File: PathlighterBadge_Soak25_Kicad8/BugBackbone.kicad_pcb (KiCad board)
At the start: 2 copper layers, 21.7 x 75.4 mm, 4 parts

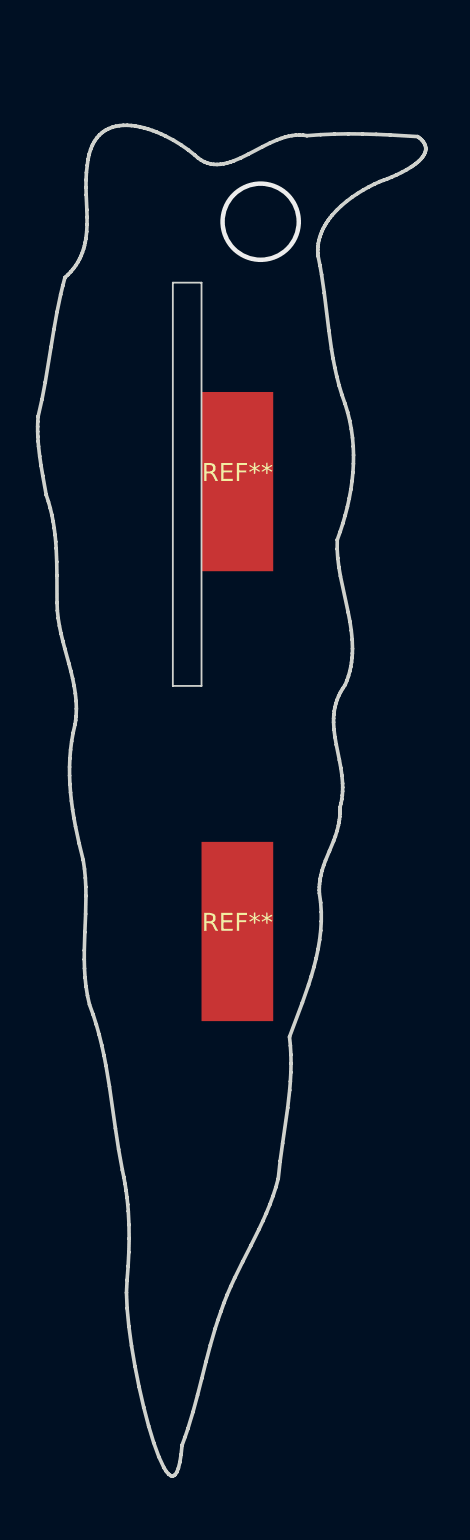
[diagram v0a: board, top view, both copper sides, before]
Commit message: Flip slots again, move logos
Slot's gotta be this way so there's room for the LED
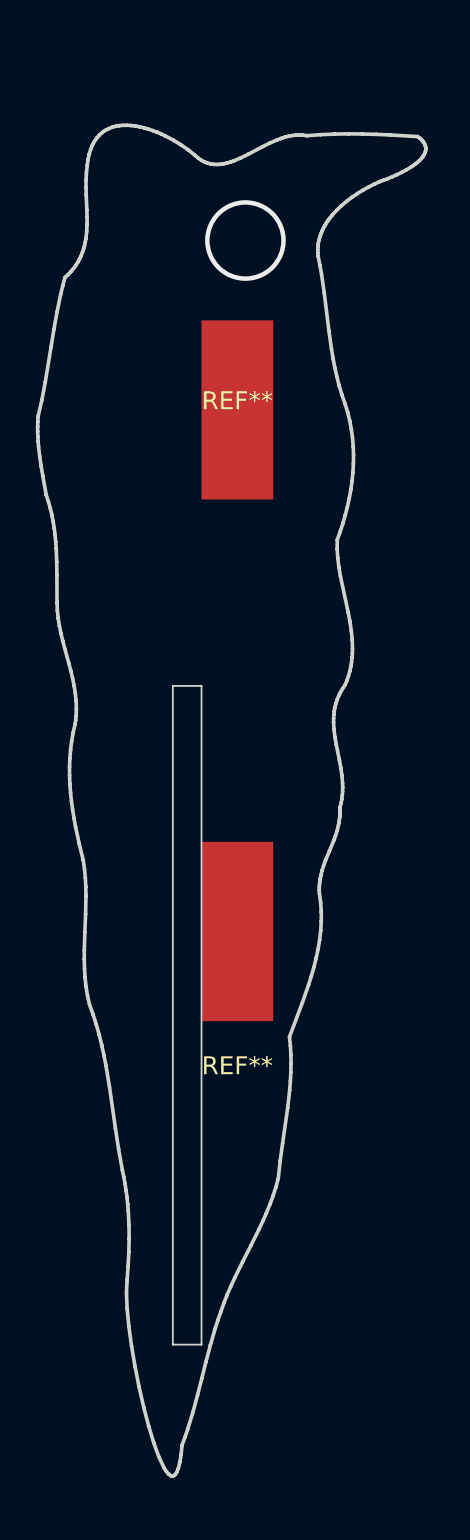
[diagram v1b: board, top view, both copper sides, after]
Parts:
- removed the ? at (108.2, 54.9)
- moved ? 67.2 mm to (105.2, 128.0)
- moved REF** 8.00 mm to (108.0, 109.0)
- moved REF** 4.00 mm to (108.0, 72.0)
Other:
- outline, holes or cut-outs redrawn
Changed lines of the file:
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@@
 (kicad_pcb
-	(version 20240108)
+	(version 20241229)
 	(generator "pcbnew")
-	(generator_version "8.0")
+	(generator_version "9.0")
 	(general
 		(thickness 1.6)
@@
 	(layers
 		(0 "F.Cu" signal)
-		(31 "B.Cu" signal)
-		(32 "B.Adhes" user "B.Adhesive")
-		(33 "F.Adhes" user "F.Adhesive")
-		(34 "B.Paste" user)
-		(35 "F.Paste" user)
-		(36 "B.SilkS" user "B.Silkscreen")
-		(37 "F.SilkS" user "F.Silkscreen")
-		(38 "B.Mask" user)
-		(39 "F.Mask" user)
-		(40 "Dwgs.User" user "User.Drawings")
-		(41 "Cmts.User" user "User.Comments")
-		(42 "Eco1.User" user "User.Eco1")
-		(43 "Eco2.User" user "User.Eco2")
-		(44 "Edge.Cuts" user)
-		(45 "Margin" user)
-		(46 "B.CrtYd" user "B.Courtyard")
-		(47 "F.CrtYd" user "F.Courtyard")
-		(48 "B.Fab" user)
-		(49 "F.Fab" user)
-		(50 "User.1" user)
-		(51 "User.2" user)
-		(52 "User.3" user)
-		(53 "User.4" user)
-		(54 "User.5" user)
-		(55 "User.6" user)
-		(56 "User.7" user)
-		(57 "User.8" user)
-		(58 "User.9" user)
+		(2 "B.Cu" signal)
+		(9 "F.Adhes" user "F.Adhesive")
+		(11 "B.Adhes" user "B.Adhesive")
+		(13 "F.Paste" user)
+		(15 "B.Paste" user)
+		(5 "F.SilkS" user "F.Silkscreen")
+		(7 "B.SilkS" user "B.Silkscreen")
+		(1 "F.Mask" user)
+		(3 "B.Mask" user)
+		(17 "Dwgs.User" user "User.Drawings")
+		(19 "Cmts.User" user "User.Comments")
+		(21 "Eco1.User" user "User.Eco1")
+		(23 "Eco2.User" user "User.Eco2")
+		(25 "Edge.Cuts" user)
+		(27 "Margin" user)
+		(31 "F.CrtYd" user "F.Courtyard")
+		(29 "B.CrtYd" user "B.Courtyard")
+		(35 "F.Fab" user)
+		(33 "B.Fab" user)
+		(39 "User.1" user)
+		(41 "User.2" user)
+		(43 "User.3" user)
+		(45 "User.4" user)
+		(47 "User.5" user)
+		(49 "User.6" user)
+		(51 "User.7" user)
+		(53 "User.8" user)
+		(55 "User.9" user)
 	)
 	(setup
 		(pad_to_mask_clearance 0)
 		(allow_soldermask_bridges_in_footprints no)
+		(tenting front back)
 		(grid_origin 105.25 85.75)
 		(pcbplotparams
-			(layerselection 0x00010fc_ffffffff)
-			(plot_on_all_layers_selection 0x0000000_00000000)
+			(layerselection 0x00000000_00000000_55555555_5755f5ff)
+			(plot_on_all_layers_selection 0x00000000_00000000_00000000_00000000)
 			(disableapertmacros no)
 			(usegerberextensions no)
@@
 			(svgprecision 4)
 			(plotframeref no)
-			(viasonmask no)
 			(mode 1)
 			(useauxorigin no)
@@
 			(pdf_front_fp_property_popups yes)
 			(pdf_back_fp_property_popups yes)
+			(pdf_metadata yes)
+			(pdf_single_document no)
 			(dxfpolygonmode yes)
 			(dxfimperialunits yes)
@@
 			(psnegative no)
 			(psa4output no)
-			(plotreference yes)
-			(plotvalue yes)
-			(plotfptext yes)
+			(plot_black_and_white yes)
 			(plotinvisibletext no)
 			(sketchpadsonfab no)
+			(plotpadnumbers no)
+			(hidednponfab no)
+			(sketchdnponfab yes)
+			(crossoutdnponfab yes)
 			(subtractmaskfromsilk no)
 			(outputformat 1)
@@
 	(footprint "adhoc:MechanicalJoint"
 		(layer "F.Cu")
-		(at 108.05 101.05)
+		(at 108.05 109.05)
 		(property "Reference" "REF**"
 			(at 0 -0.5 0)
@@
 			(unlocked yes)
 			(layer "F.Fab")
-			(effects
-				(font
-					(size 1 1)
-					(thickness 0.15)
-				)
-			)
-		)
-		(property "Footprint" "adhoc:MechanicalJoint"
-			(at 0 0 0)
-			(unlocked yes)
-			(layer "F.Fab")
-			(hide yes)
 			(effects
 				(font
@@
 		)
 		(pad "" smd rect
-			(at 0 0)
+			(at 0 -8)
 			(size 4 10)
-			(layers "F.Cu" "F.Paste" "F.Mask")
-		)
+			(layers "F.Cu" "F.Mask" "F.Paste")
+		)
+		(embedded_fonts no)
 	)
 	(footprint "adhoc:Slot_1.6mm"
 		(layer "F.Cu")
-		(at 108.25 54.85 135)
+		(at 105.25 128)
 		(property "Reference" ""
-			(at 0 0 135)
+			(at 0 0 0)
 			(layer "F.SilkS")
 			(effects
@@
 		)
 		(property "Value" ""
-			(at 0 0 135)
-			(layer "F.Fab")
-			(effects
-				(font
-					(size 1.27 1.27)
-					(thickness 0.15)
-				)
-			)
-		)
-		(property "Footprint" "adhoc:Slot_1.6mm"
-			(at 0 0 135)
-			(layer "F.Fab")
-			(hide yes)
-			(effects
-				(font
-					(size 1.27 1.27)
-					(thickness 0.15)
-				)
-			)
-		)
-		(property "Datasheet" ""
-			(at 0 0 135)
-			(layer "F.Fab")
-			(hide yes)
-			(effects
-				(font
-					(size 1.27 1.27)
-					(thickness 0.15)
-				)
-			)
-		)
-		(property "Description" ""
-			(at 0 0 135)
-			(layer "F.Fab")
-			(hide yes)
-			(effects
-				(font
-					(size 1.27 1.27)
-					(thickness 0.15)
-				)
-			)
-		)
-		(pad "" np_thru_hole circle
-			(at 0 0 135)
-			(size 1.6 1.6)
-			(drill oval 1.6 10)
-			(layers "*.Cu" "*.Mask" "In1.Cu" "In2.Cu" "In3.Cu" "In4.Cu" "In5.Cu" "In6.Cu"
-				"In7.Cu" "In8.Cu" "In9.Cu" "In10.Cu" "In11.Cu" "In12.Cu" "In13.Cu" "In14.Cu"
-				"In15.Cu" "In16.Cu" "In17.Cu" "In18.Cu" "In19.Cu" "In20.Cu" "In21.Cu"
-				"In22.Cu" "In23.Cu" "In24.Cu" "In25.Cu" "In26.Cu" "In27.Cu" "In28.Cu"
-				"In29.Cu" "In30.Cu"
-			)
-		)
-	)
-	(footprint "adhoc:Slot_1.6mm"
-		(layer "F.Cu")
-		(at 105.25 60.75)
-		(property "Reference" ""
-			(at 0 0 0)
-			(layer "F.SilkS")
-			(effects
-				(font
-					(size 1.27 1.27)
-					(thickness 0.15)
-				)
-			)
-		)
-		(property "Value" ""
-			(at 0 0 0)
-			(layer "F.Fab")
-			(effects
-				(font
-					(size 1.27 1.27)
-					(thickness 0.15)
-				)
-			)
-		)
-		(property "Footprint" "adhoc:Slot_1.6mm"
-			(at 0 0 0)
-			(layer "F.Fab")
-			(hide yes)
+			(at 0 0 0)
+			(layer "F.Fab")
 			(effects
 				(font
@@
 			(size 1.6 1.6)
 			(drill oval 1.6 10)
-			(layers "*.Cu" "*.Mask" "In1.Cu" "In2.Cu" "In3.Cu" "In4.Cu" "In5.Cu" "In6.Cu"
-				"In7.Cu" "In8.Cu" "In9.Cu" "In10.Cu" "In11.Cu" "In12.Cu" "In13.Cu" "In14.Cu"
-				"In15.Cu" "In16.Cu" "In17.Cu" "In18.Cu" "In19.Cu" "In20.Cu" "In21.Cu"
-				"In22.Cu" "In23.Cu" "In24.Cu" "In25.Cu" "In26.Cu" "In27.Cu" "In28.Cu"
-				"In29.Cu" "In30.Cu"
-			)
-		)
+			(layers "*.Cu" "*.Mask")
+		)
+		(embedded_fonts no)
 	)
 	(footprint "adhoc:MechanicalJoint"
 		(layer "F.Cu")
-		(at 108.05 75.95)
+		(at 108.05 71.95)
 		(property "Reference" "REF**"
 			(at 0 -0.5 0)
@@
 			(unlocked yes)
 			(layer "F.Fab")
-			(effects
-				(font
-					(size 1 1)
-					(thickness 0.15)
-				)
-			)
-		)
-		(property "Footprint" "adhoc:MechanicalJoint"
-			(at 0 0 0)
-			(unlocked yes)
-			(layer "F.Fab")
-			(hide yes)
 			(effects
 				(font
@@
 			(at 0 0)
 			(size 4 10)
-			(layers "F.Cu" "F.Paste" "F.Mask")
-		)
+			(layers "F.Cu" "F.Mask" "F.Paste")
+		)
+		(embedded_fonts no)
 	)
 	(gr_poly
@@
 			(type solid)
 		)
-		(fill none)
+		(fill no)
 		(layer "Edge.Cuts")
 	)
 	(gr_rect
-		(start 104.45 64.85)
-		(end 106.05 87.35)
+		(start 104.45 87.35)
+		(end 106.05 124.1)
 		(stroke
 			(width 0.1)
 			(type default)
 		)
-		(fill none)
+		(fill no)
 		(layer "Edge.Cuts")
 	)
 	(via
-		(at 109.35 61.45)
+		(at 108.5 62.5)
 		(size 4.5)
 		(drill 4)
@@
 		(net 0)
 	)
+	(embedded_fonts no)
 )

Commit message: Rework backbone
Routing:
- added copper zone on F.Cu, net (none)
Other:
- board size 21.7 x 75.4 mm -> 22 x 75.3 mm

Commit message: Tweaks from feedback
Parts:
- removed the REF** at (108.0, 109.0)
- added REF**: MechanicalJoint, footprints:MechanicalJoint, B.Cu at (108.0, 97.5)
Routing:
- removed copper zone on F.Cu, net (none)
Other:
- board size 22 x 75.3 mm -> 22 x 71.3 mm

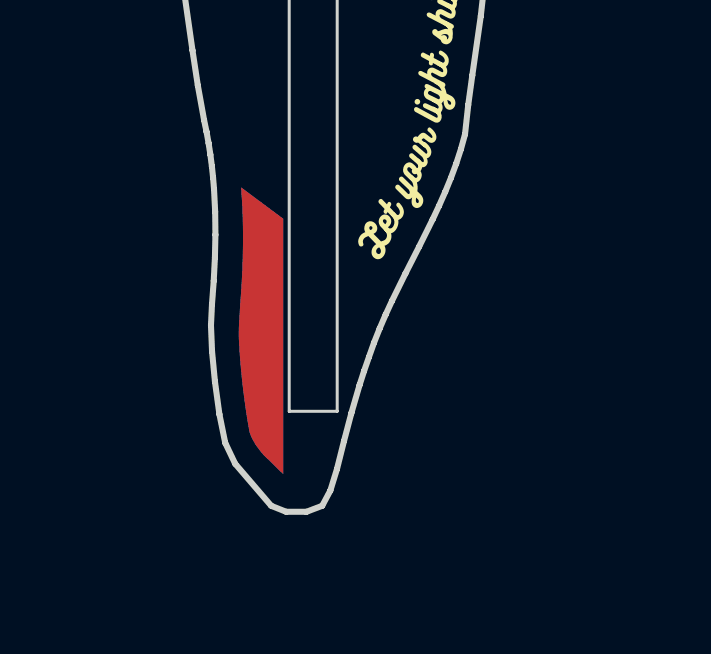
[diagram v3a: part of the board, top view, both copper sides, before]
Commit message: Fix overlap on G/C, adjust backbone bands
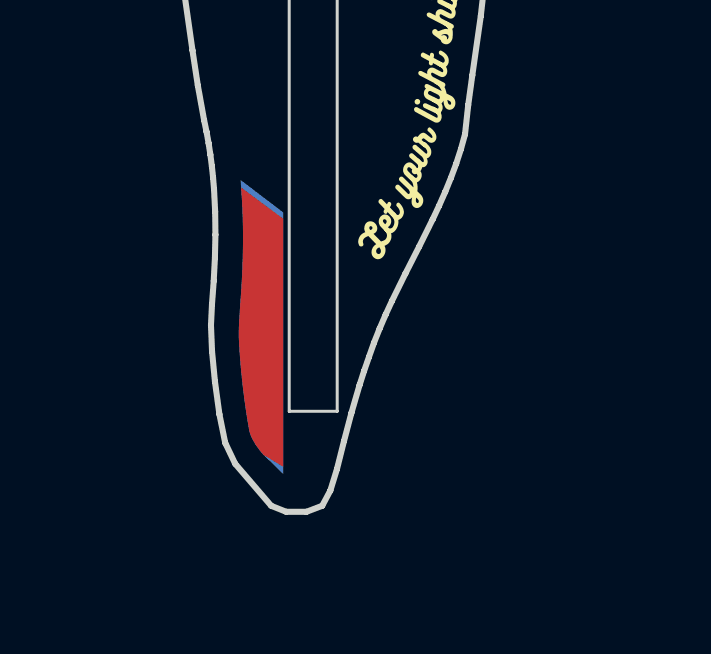
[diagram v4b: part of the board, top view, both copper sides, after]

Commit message: Final tweaks, hopefully!
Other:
- board size 22 x 71.3 mm -> 18.6 x 70.3 mm

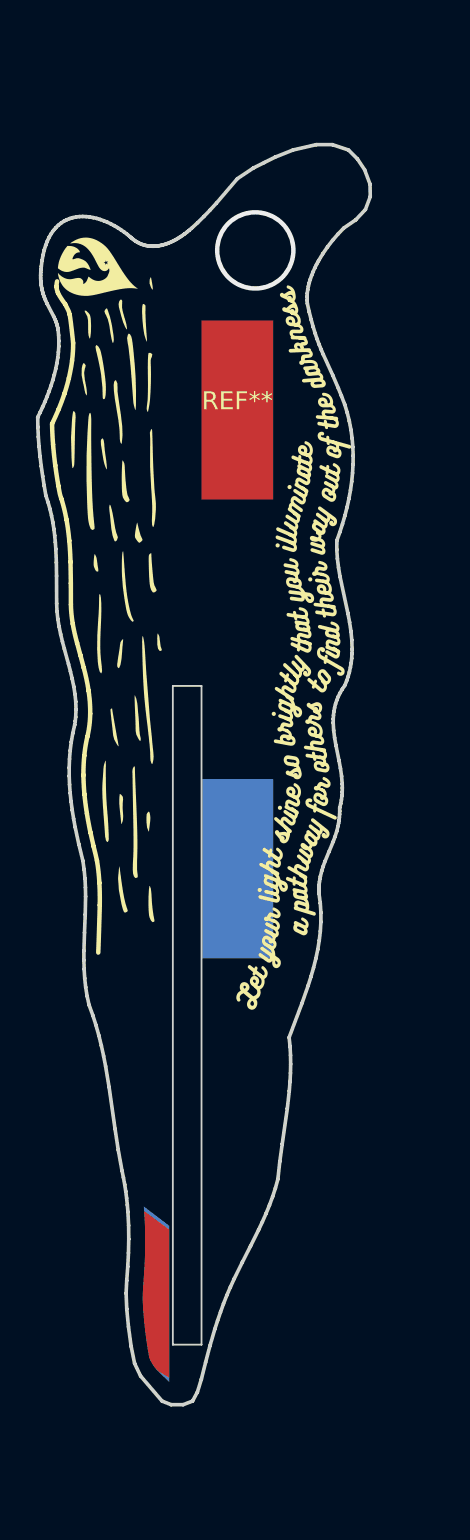
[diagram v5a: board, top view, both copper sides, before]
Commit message: Lots of little tweaks getting ready for production
Rerouting traces, baking board outlines without the weird bits,
adding silkscreen bits, generally polishing
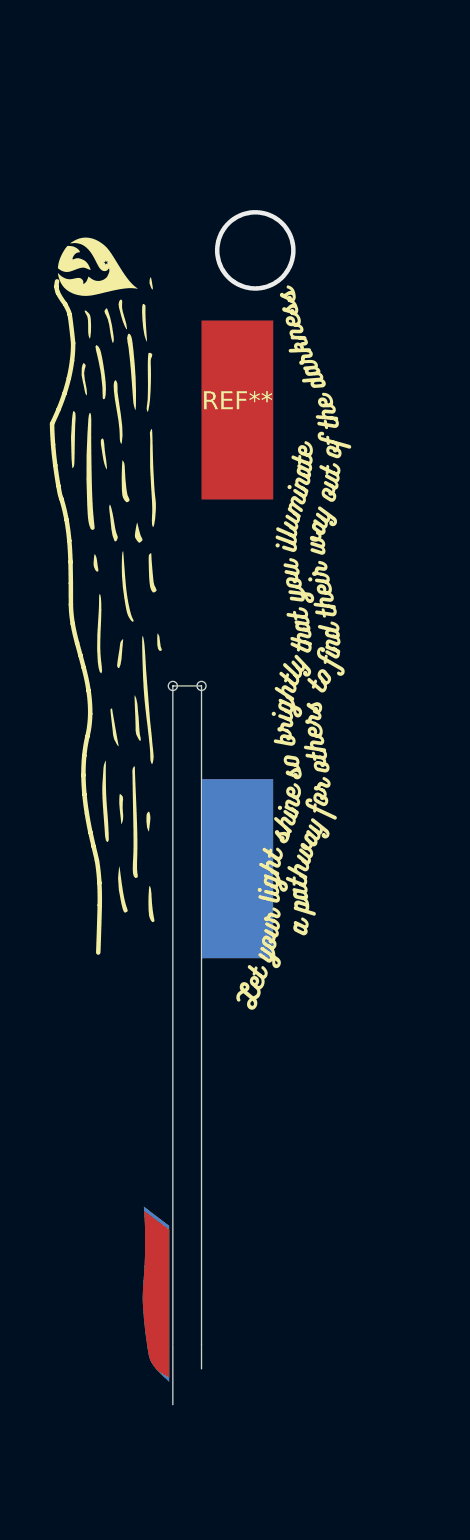
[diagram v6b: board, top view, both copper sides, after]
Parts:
- removed ?: , adhoc:Slot_1.6mm
- added REF**: NPTH_20mil, footprints:NPTH_20mil, F.Cu at (106.0, 87.3)
- added REF**: NPTH_20mil, footprints:NPTH_20mil, F.Cu at (104.5, 87.3)
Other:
- board size 18.6 x 70.3 mm -> 1.6 x 40.1 mm

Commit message: Fix Edge.Cuts on backbone
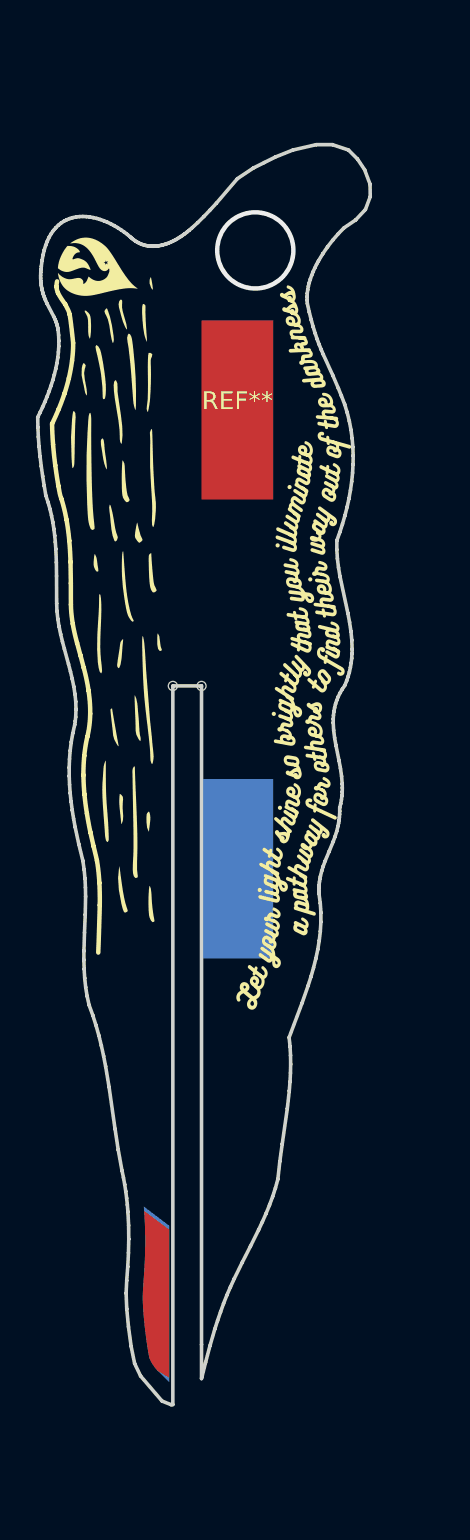
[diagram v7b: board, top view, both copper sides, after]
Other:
- board size 1.6 x 40.1 mm -> 18.6 x 70.3 mm
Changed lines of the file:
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@@
 		)
 		(fill no)
-		(layer "Dwgs.User")
-	)
-	(gr_line
-		(start 104.45 87.35)
-		(end 106.05 87.35)
-		(stroke
-			(width 0.05)
-			(type default)
-		)
 		(layer "Edge.Cuts")
 	)
-	(gr_line
-		(start 106.05 87.35)
-		(end 106.05 124.1)
-		(stroke
-			(width 0.05)
-			(type default)
-		)
-		(layer "Edge.Cuts")
-	)
-	(gr_line
-		(start 104.45 127.45)
-		(end 104.45 124.1)
-		(stroke
-			(width 0.05)
-			(type default)
-		)
-		(layer "Edge.Cuts")
-	)
-	(gr_line
-		(start 104.45 87.35)
-		(end 104.45 124.05)
-		(stroke
-			(width 0.05)
-			(type default)
-		)
-		(layer "Edge.Cuts")
-	)
-	(gr_line
-		(start 106.05 124.1)
-		(end 106.05 125.45)
-		(stroke
-			(width 0.05)
-			(type default)
-		)
-		(layer "Edge.Cuts")
-	)

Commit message: More final tweaks of some sort
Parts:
- moved REF** 0.38 mm to (108.4, 97.5)
